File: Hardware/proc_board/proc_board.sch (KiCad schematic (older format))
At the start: 12 parts, among them J1 Conn_01x40, U1 74HC21, U2 W65C02SxP, U3 HM62256BLP, U4 28C256, U5 74HC00

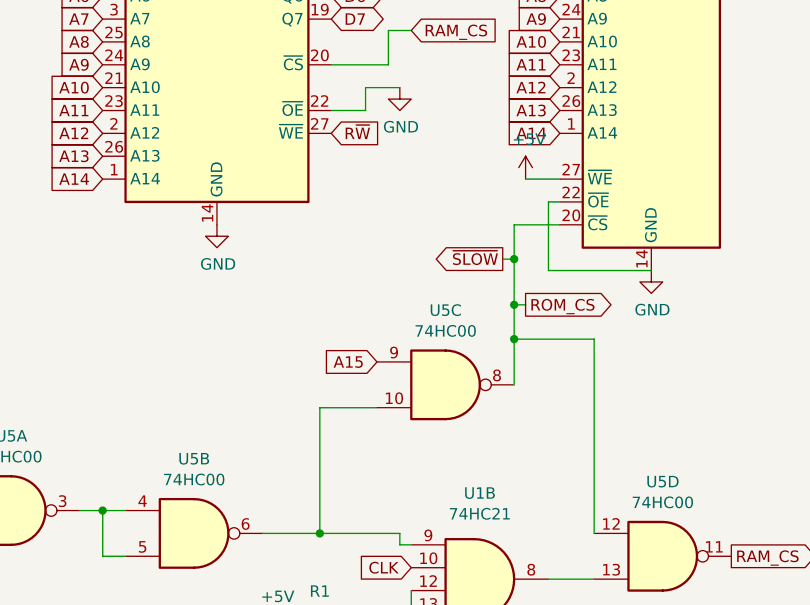
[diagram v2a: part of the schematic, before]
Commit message: Many updates. SLOW signal is now shared amongst all slots, so their output has to be open drain.
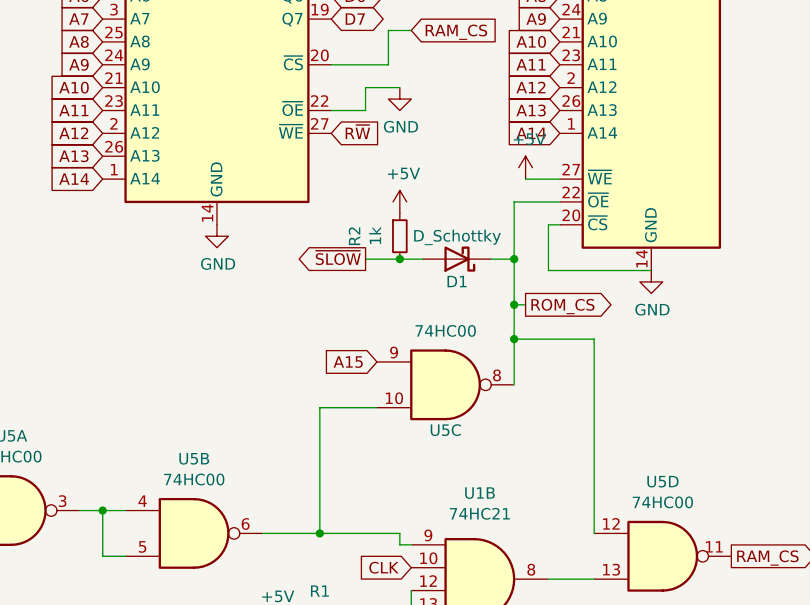
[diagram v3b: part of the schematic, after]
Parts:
- added D1: D_Schottky, Diode_SMD:D_0805_2012Metric_Pad1.15x1.40mm_HandSolder, symbol Device:D_Schottky
- added R2: 1k, Resistor_SMD:R_0805_2012Metric_Pad1.15x1.40mm_HandSolder, symbol Device:R_Small
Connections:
- net +5V: now also R2.1
- net GND: now also U4.20 (~CS); no longer U4.22 (~OE)
- net ROM_CS: now also U4.22 (~OE), D1.1 (K); no longer J1.22 (Pin_22), U4.20 (~CS)
- new net ~SLOW~: D1.2 (A), J1.22 (Pin_22), R2.2
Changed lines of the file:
@@
 U 3 1 5FDF1828
 P 8600 5050
-F 0 "U5" H 8600 5375 50  0000 C CNN
+F 0 "U5" H 8600 4850 50  0000 C CNN
 F 1 "74HC00" H 8600 5284 50  0000 C CNN
 F 2 "Package_DIP:DIP-14_W7.62mm_Socket" H 8600 5050 50  0001 C CNN
@@
 Wire Wire Line
 	9100 4150 8950 4150
-Wire Wire Line
-	9100 4250 9050 4250
-Wire Wire Line
-	9050 4250 9050 4550
 Wire Wire Line
 	9050 4550 9500 4550
@@
 Text GLabel 9900 3250 2    50   BiDi ~ 0
 D7
-Wire Wire Line
-	8900 4350 9100 4350
 Text GLabel 6400 5500 0    50   Input ~ 0
 ~SSEL~
@@
 RAM_CS
 Wire Wire Line
-	8900 4350 8900 4500
-Wire Wire Line
 	8450 5750 8400 5750
 Wire Wire Line
@@
 	1    0    0    -1
 $EndComp
-Text GLabel 8850 4500 0    50   Output ~ 0
+Text GLabel 8250 4500 0    50   Output ~ 0
 ~SLOW~
-Wire Wire Line
-	8850 4500 8900 4500
 Connection ~ 8900 4500
 Wire Wire Line
 	8900 4500 8900 4700
+Wire Wire Line
+	9050 4550 9050 4350
+Wire Wire Line
+	9050 4350 9100 4350
+Wire Wire Line
+	8900 4250 9100 4250
+Wire Wire Line
+	8900 4250 8900 4500
+$Comp
+L Device:D_Schottky D1
+U 1 1 601C82E8
+P 8650 4500
+F 0 "D1" H 8650 4600 50  0000 C CNN
+F 1 "D_Schottky" H 8650 4400 50  0000 C CNN
+F 2 "Diode_SMD:D_0805_2012Metric_Pad1.15x1.40mm_HandSolder" H 8650 4500 50  0001 C CNN
+F 3 "~" H 8650 4500 50  0001 C CNN
+	1    8650 4500
+	-1   0    0    1
+$EndComp
+Wire Wire Line
+	8800 4500 8900 4500
+$Comp
+L Device:R_Small R2
+U 1 1 601D19CD
+P 8400 4400
+F 0 "R2" V 8204 4400 50  0000 C CNN
+F 1 "1k" V 8295 4400 50  0000 C CNN
+F 2 "Resistor_SMD:R_0805_2012Metric_Pad1.15x1.40mm_HandSolder" H 8400 4400 50  0001 C CNN
+F 3 "~" H 8400 4400 50  0001 C CNN
+	1    8400 4400
+	1    0    0    -1
+$EndComp
+$Comp
+L power:+5V #PWR0123
+U 1 1 601D30DC
+P 8400 4300
+F 0 "#PWR0123" H 8400 4150 50  0001 C CNN
+F 1 "+5V" H 8415 4473 50  0000 C CNN
+F 2 "" H 8400 4300 50  0001 C CNN
+F 3 "" H 8400 4300 50  0001 C CNN
+	1    8400 4300
+	1    0    0    -1
+$EndComp
+Wire Wire Line
+	8500 4500 8400 4500
+Connection ~ 8400 4500
+Wire Wire Line
+	8400 4500 8250 4500
 $EndSCHEMATC

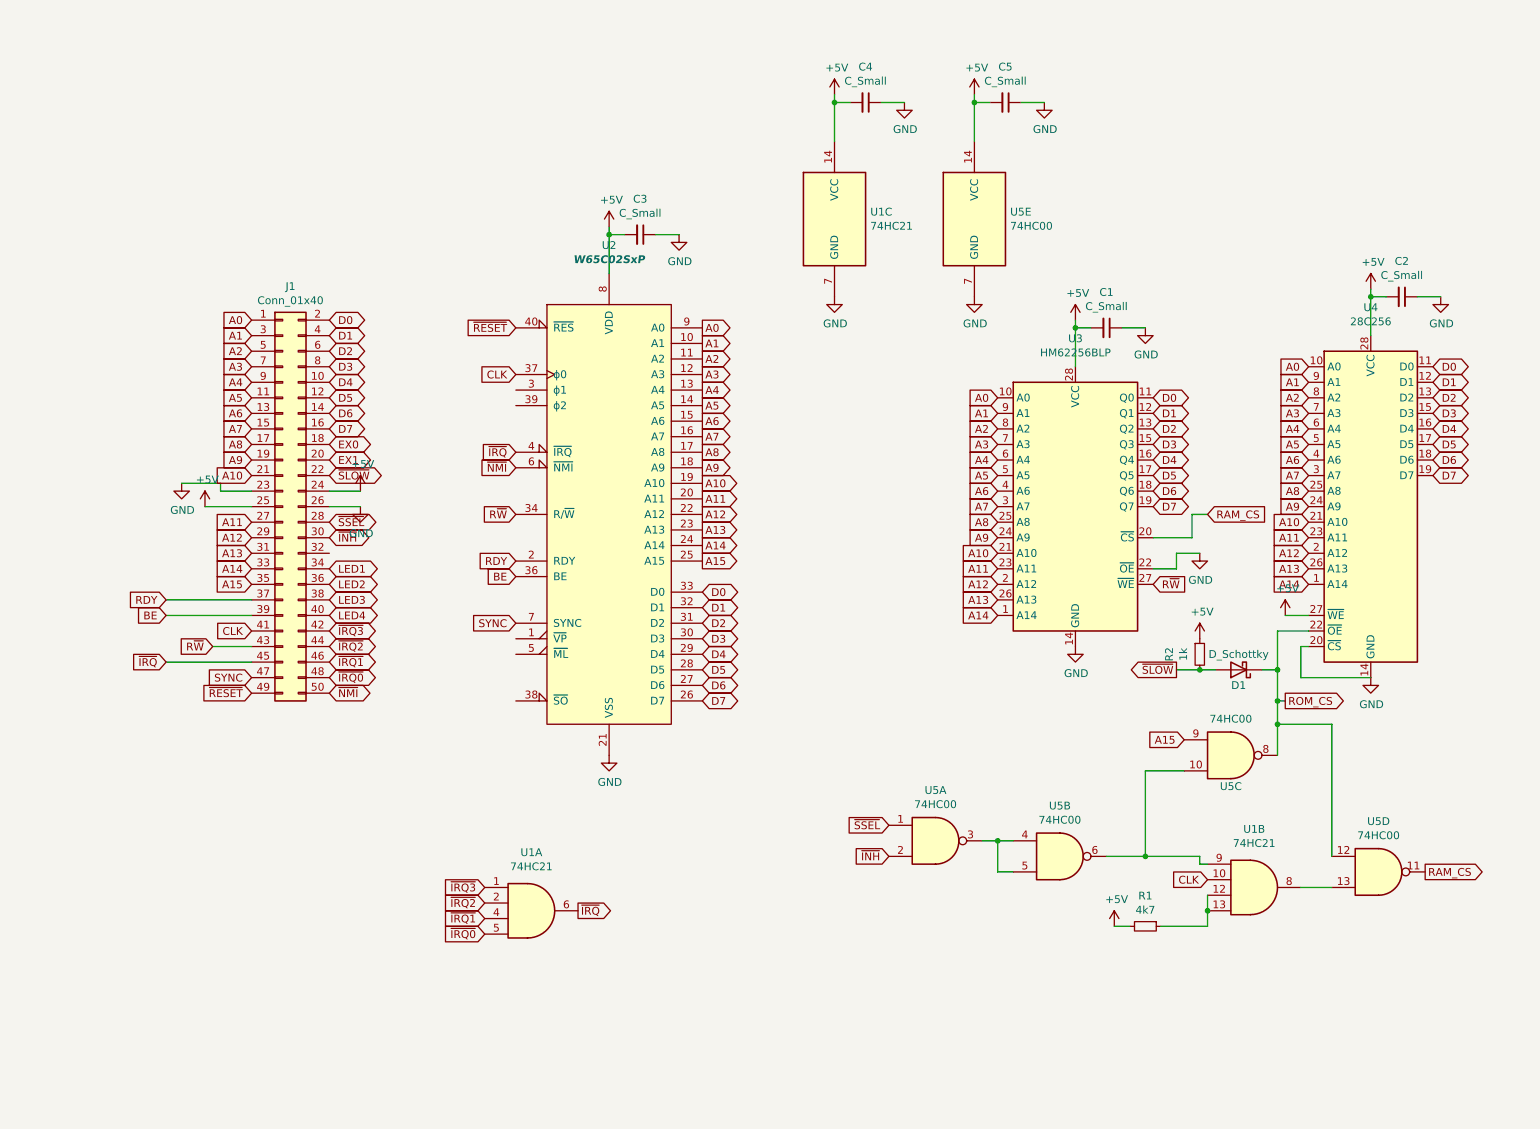
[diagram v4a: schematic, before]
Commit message: update CPU board address decoding with a 16V8
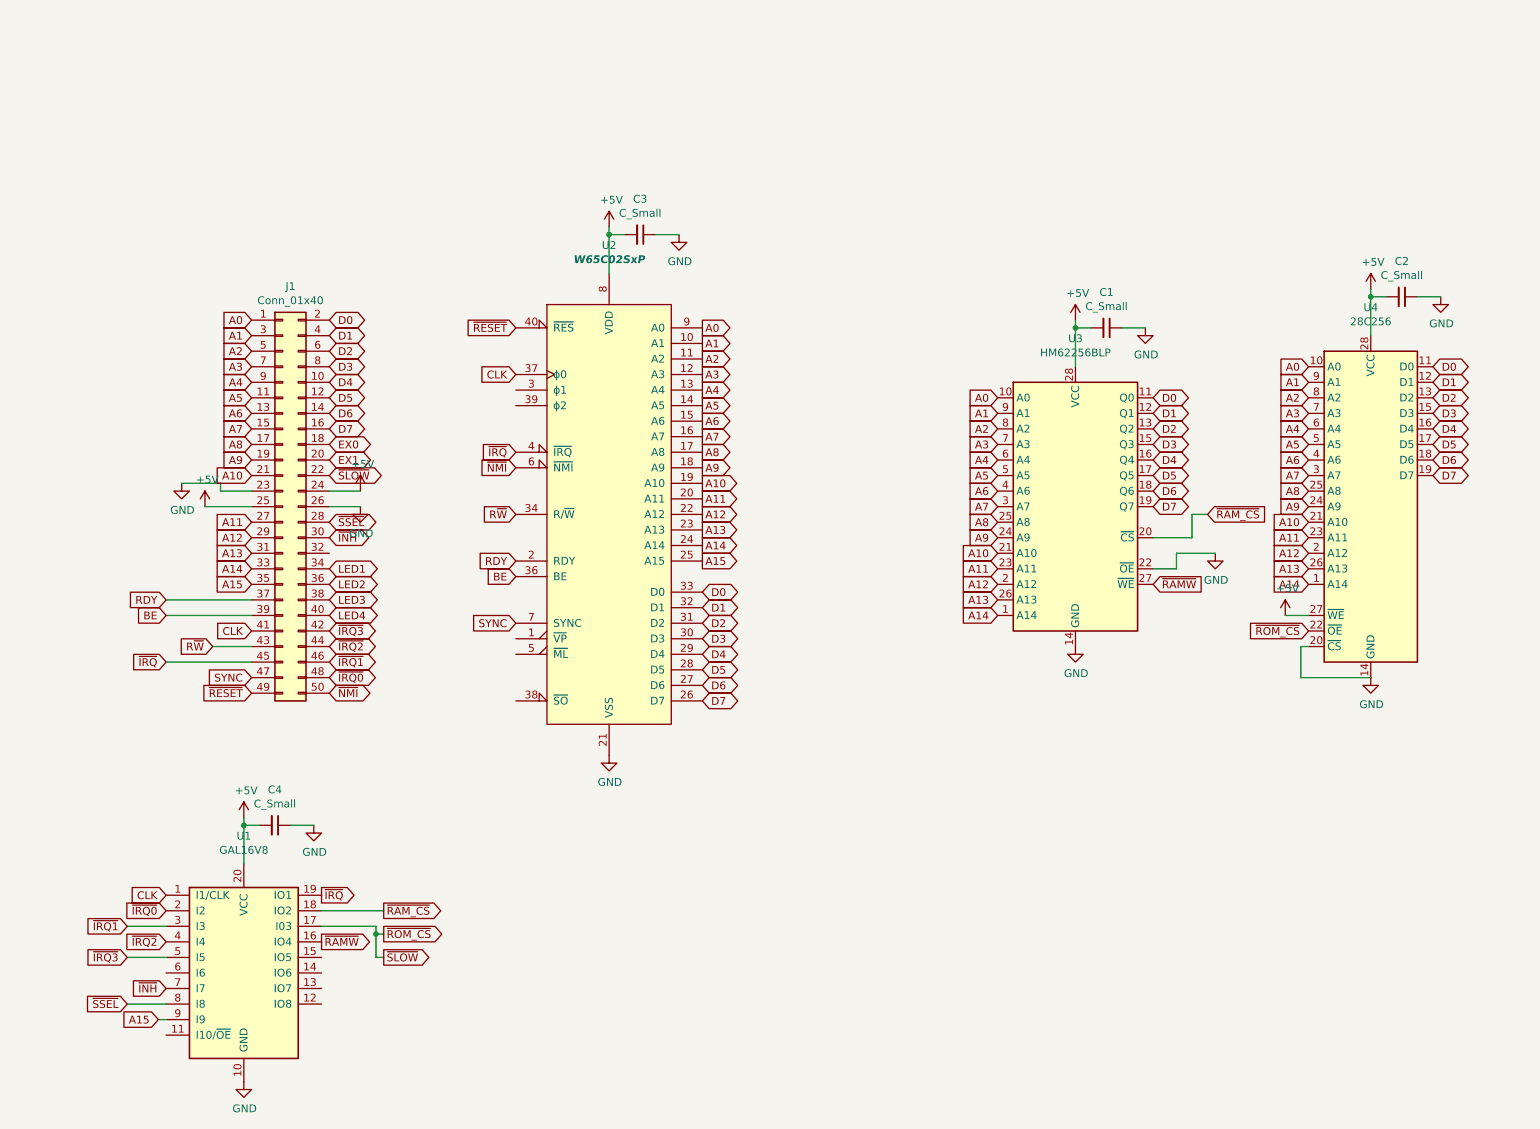
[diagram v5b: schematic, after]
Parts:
- removed C5: C_Small, Capacitor_SMD:C_1206_3216Metric_Pad1.42x1.75mm_HandSolder, symbol Device:C_Small
- removed D1: D_Schottky, Diode_SMD:D_0805_2012Metric_Pad1.15x1.40mm_HandSolder, symbol Device:D_Schottky
- removed R1: 4k7, Resistor_SMD:R_0805_2012Metric_Pad1.15x1.40mm_HandSolder, symbol Device:R_Small
- removed R2: 1k, Resistor_SMD:R_0805_2012Metric_Pad1.15x1.40mm_HandSolder, symbol Device:R_Small
- removed U1: 74HC21, Package_DIP:DIP-14_W7.62mm_Socket, symbol 74xx:74LS21
- removed U5: 74HC00, Package_DIP:DIP-14_W7.62mm_Socket, symbol 74xx:74HC00
- added U1: GAL16V8, Package_DIP:DIP-20_W7.62mm_Socket, symbol Logic_Programmable:GAL16V8
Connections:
- net ~SLOW~ is gone; now on net ~ROM_CS~: J1.22 (Pin_22)
- net +5V: now also U1.20 (VCC)
- net A15: now also U1.9 (I9)
- net CLK: now also U1.1 (I1/CLK)
- net GND: now also U1.10 (GND)
- net R~W~: no longer U3.27 (~WE)
- net ~INH~: now also U1.7 (I7)
- net ~IRQ0~: now also U1.2 (I2)
- net ~IRQ1~: now also U1.3 (I3)
- net ~IRQ2~: now also U1.4 (I4)
- net ~IRQ3~: now also U1.5 (I5)
- net ~IRQ~: now also U1.19 (IO1)
- net ~SSEL~: now also U1.8 (I8)
- net RAM_CS renamed ~RAM_CS~
- net ~RAM_CS~: now also U1.18 (IO2)
- net ROM_CS renamed ~ROM_CS~
- net ~ROM_CS~: now also U1.17 (I03)
- new net ~RAMW~: U1.16 (IO4), U3.27 (~WE)

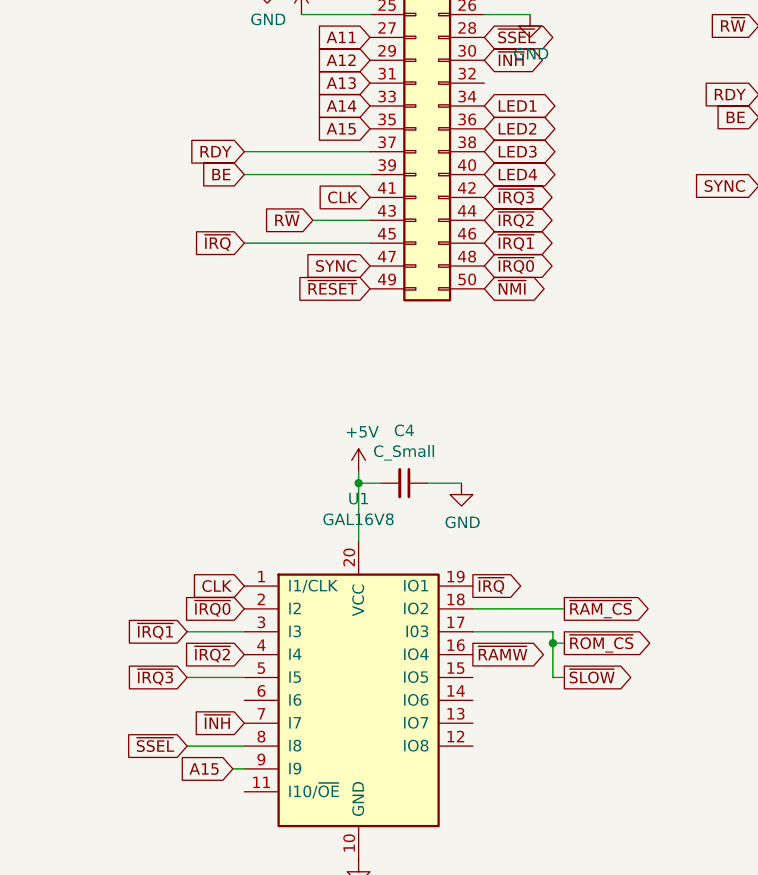
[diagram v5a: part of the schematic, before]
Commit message: Add IRQ signal for Slot 5
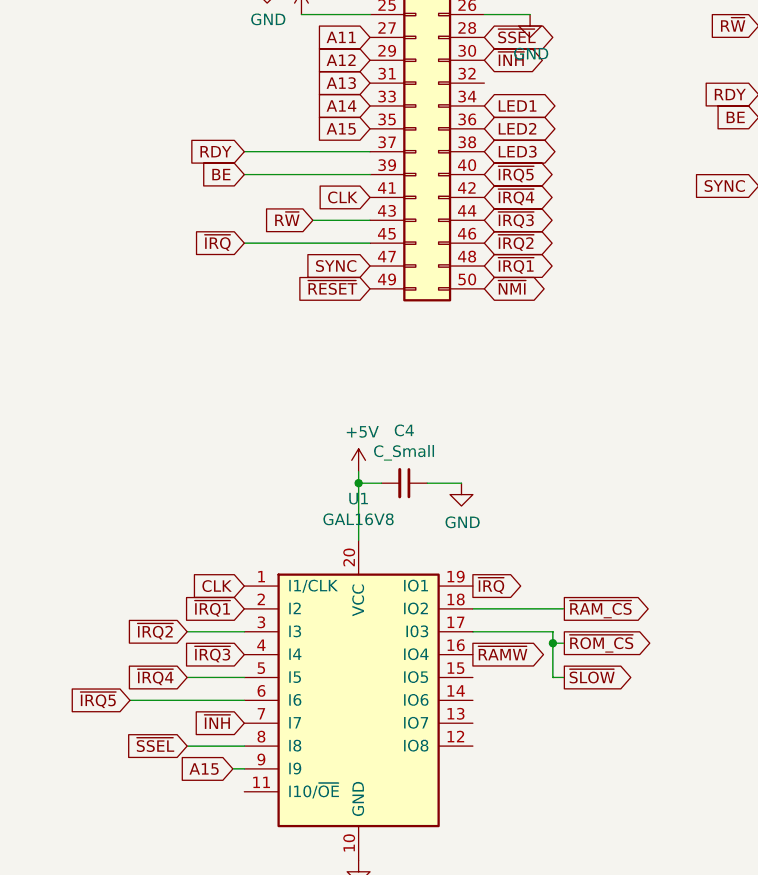
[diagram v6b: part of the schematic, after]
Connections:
- net LED4 is gone; now on net ~IRQ5~: J1.40 (Pin_40)
- net ~IRQ0~ is gone; now on net ~IRQ1~: J1.48 (Pin_48), U1.2 (I2)
- net ~IRQ1~: no longer J1.46 (Pin_46), U1.3 (I3)
- net ~IRQ2~: now also J1.46 (Pin_46), U1.3 (I3); no longer J1.44 (Pin_44), U1.4 (I4)
- net ~IRQ3~: now also J1.44 (Pin_44), U1.4 (I4); no longer J1.42 (Pin_42), U1.5 (I5)
- net ~IRQ5~: now reaches U1.6 (I6)
- new net ~IRQ4~: J1.42 (Pin_42), U1.5 (I5)
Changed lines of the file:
@@
 ~IRQ~
 Text GLabel 2800 4550 2    50   BiDi ~ 0
-~IRQ0~
+~IRQ1~
 Text GLabel 2800 4450 2    50   BiDi ~ 0
-~IRQ1~
+~IRQ2~
 Text GLabel 2800 4350 2    50   BiDi ~ 0
-~IRQ2~
+~IRQ3~
 Text GLabel 2800 4250 2    50   BiDi ~ 0
-~IRQ3~
+~IRQ4~
 Wire Wire Line
 	1750 4450 2300 4450
@@
 LED3
 Text GLabel 2800 4150 2    50   BiDi ~ 0
-LED4
+~IRQ5~
 Text GLabel 2800 3050 2    50   BiDi ~ 0
 EX0
@@
 CLK
 Text GLabel 1750 6050 0    50   Input ~ 0
-~IRQ0~
+~IRQ1~
 Text GLabel 1500 6150 0    50   Input ~ 0
-~IRQ1~
+~IRQ2~
 Text GLabel 1750 6250 0    50   Input ~ 0
-~IRQ2~
+~IRQ3~
 Text GLabel 1500 6350 0    50   Input ~ 0
-~IRQ3~
+~IRQ4~
 Text GLabel 2750 5950 2    50   Output ~ 0
 ~IRQ~
@@
 	1    0    0    -1
 $EndComp
+Text GLabel 1250 6450 0    50   Input ~ 0
+~IRQ5~
+Wire Wire Line
+	1750 6450 1250 6450
 $EndSCHEMATC

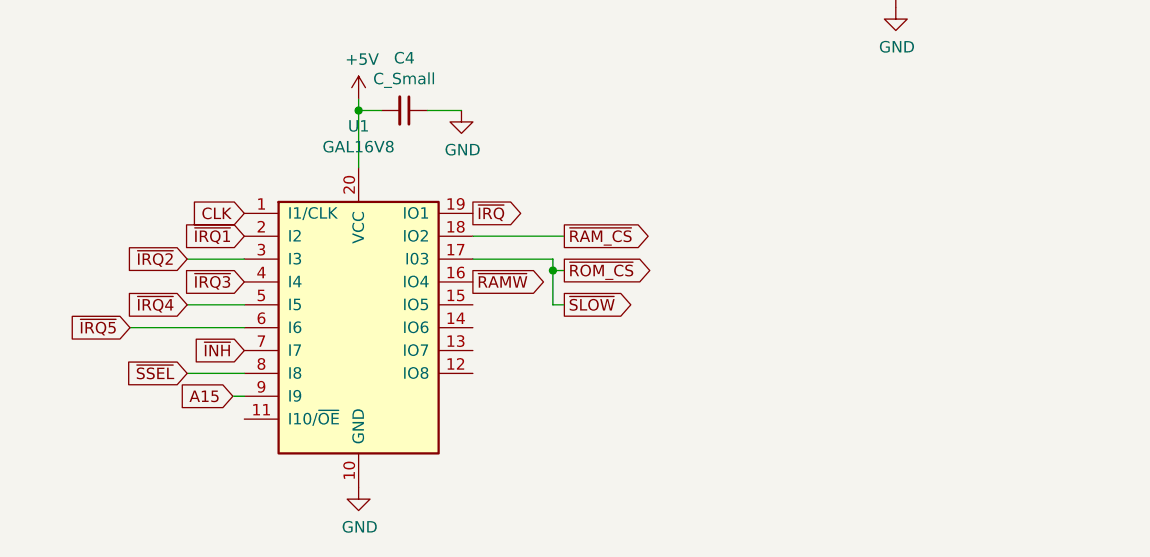
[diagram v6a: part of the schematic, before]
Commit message: Add RW signal to 16V8 inputs. Add diode and pullup resistor to SLOW output signal to make it open collector so that it can be wire ored with the SLOW signal coming from other boards.
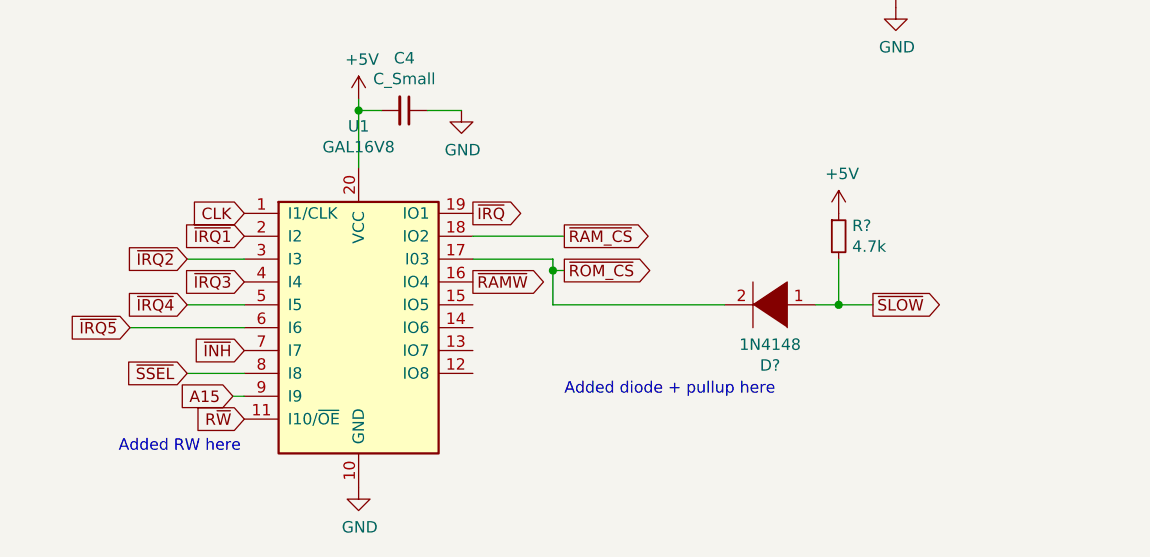
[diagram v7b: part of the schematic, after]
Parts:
- added D?: 1N4148, Diode_THT:D_DO-35_SOD27_P7.62mm_Horizontal, symbol pspice:DIODE
- added R?: 4.7k, Resistor_SMD:R_0805_2012Metric_Pad1.15x1.40mm_HandSolder, symbol Device:R_Small
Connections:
- net +5V: now also R?.1
- net R~W~: now also U1.11 (I10/~OE~)
- net ~ROM_CS~: now also D?.2 (A); no longer J1.22 (Pin_22)
- new net ~SLOW~: D?.1 (K), J1.22 (Pin_22), R?.2
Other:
- note added: "Added RW here"
- note added: "Added diode + pullup here"
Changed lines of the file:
@@
 Text GLabel 3150 6200 2    50   Output ~ 0
 ~ROM_CS~
-Text GLabel 3150 6350 2    50   Output ~ 0
+Text GLabel 4500 6350 2    50   Output ~ 0
 ~SLOW~
-Wire Wire Line
-	3150 6350 3100 6350
 Wire Wire Line
 	3100 6350 3100 6200
@@
 Wire Wire Line
 	1750 6450 1250 6450
+Text GLabel 1750 6850 0    50   Input ~ 0
+R~W~
+Text Notes 1200 7000 0    50   ~ 0
+Added RW here
+Text Notes 3150 6750 0    50   ~ 0
+Added diode + pullup here
+$Comp
+L pspice:DIODE D?
+U 1 1 60359E86
+P 4050 6350
+F 0 "D?" H 4050 6615 50  0000 C CNN
+F 1 "1N4148" H 4050 6524 50  0000 C CNN
+F 2 "Diode_THT:D_DO-35_SOD27_P7.62mm_Horizontal" H 4050 6350 50  0001 C CNN
+F 3 "~" H 4050 6350 50  0001 C CNN
+	1    4050 6350
+	-1   0    0    1
+$EndComp
+Wire Wire Line
+	4500 6350 4350 6350
+Wire Wire Line
+	3100 6350 3850 6350
+$Comp
+L Device:R_Small R?
+U 1 1 6035C6C6
+P 4350 6050
+F 0 "R?" H 4409 6096 50  0000 L CNN
+F 1 "4.7k" H 4409 6005 50  0000 L CNN
+F 2 "Resistor_SMD:R_0805_2012Metric_Pad1.15x1.40mm_HandSolder" H 4350 6050 50  0001 C CNN
+F 3 "~" H 4350 6050 50  0001 C CNN
+	1    4350 6050
+	1    0    0    -1
+$EndComp
+$Comp
+L power:+5V #PWR?
+U 1 1 6035CE86
+P 4350 5950
+F 0 "#PWR?" H 4350 5800 50  0001 C CNN
+F 1 "+5V" H 4365 6123 50  0000 C CNN
+F 2 "" H 4350 5950 50  0001 C CNN
+F 3 "" H 4350 5950 50  0001 C CNN
+	1    4350 5950
+	1    0    0    -1
+$EndComp
+Wire Wire Line
+	4350 6150 4350 6350
+Connection ~ 4350 6350
+Wire Wire Line
+	4350 6350 4250 6350
 $EndSCHEMATC
